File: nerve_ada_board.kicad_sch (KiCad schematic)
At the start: 55 parts, among them J2 TC2050-IDC, J3 2171750001, J4 Camera, J5 CAN1, J6 CAN2, J7 WS2812B, SW1 SPST, SW2 SPST, SW3 SPDT, SW4 SPST, U1 LD1117S33TR_SOT223, U2 STM32F446RET, U5 XBP9B-DMWT-002, U6 SAM-M10Q, U9 TXB0102DCT, Y1 8M, Y2 32.768K

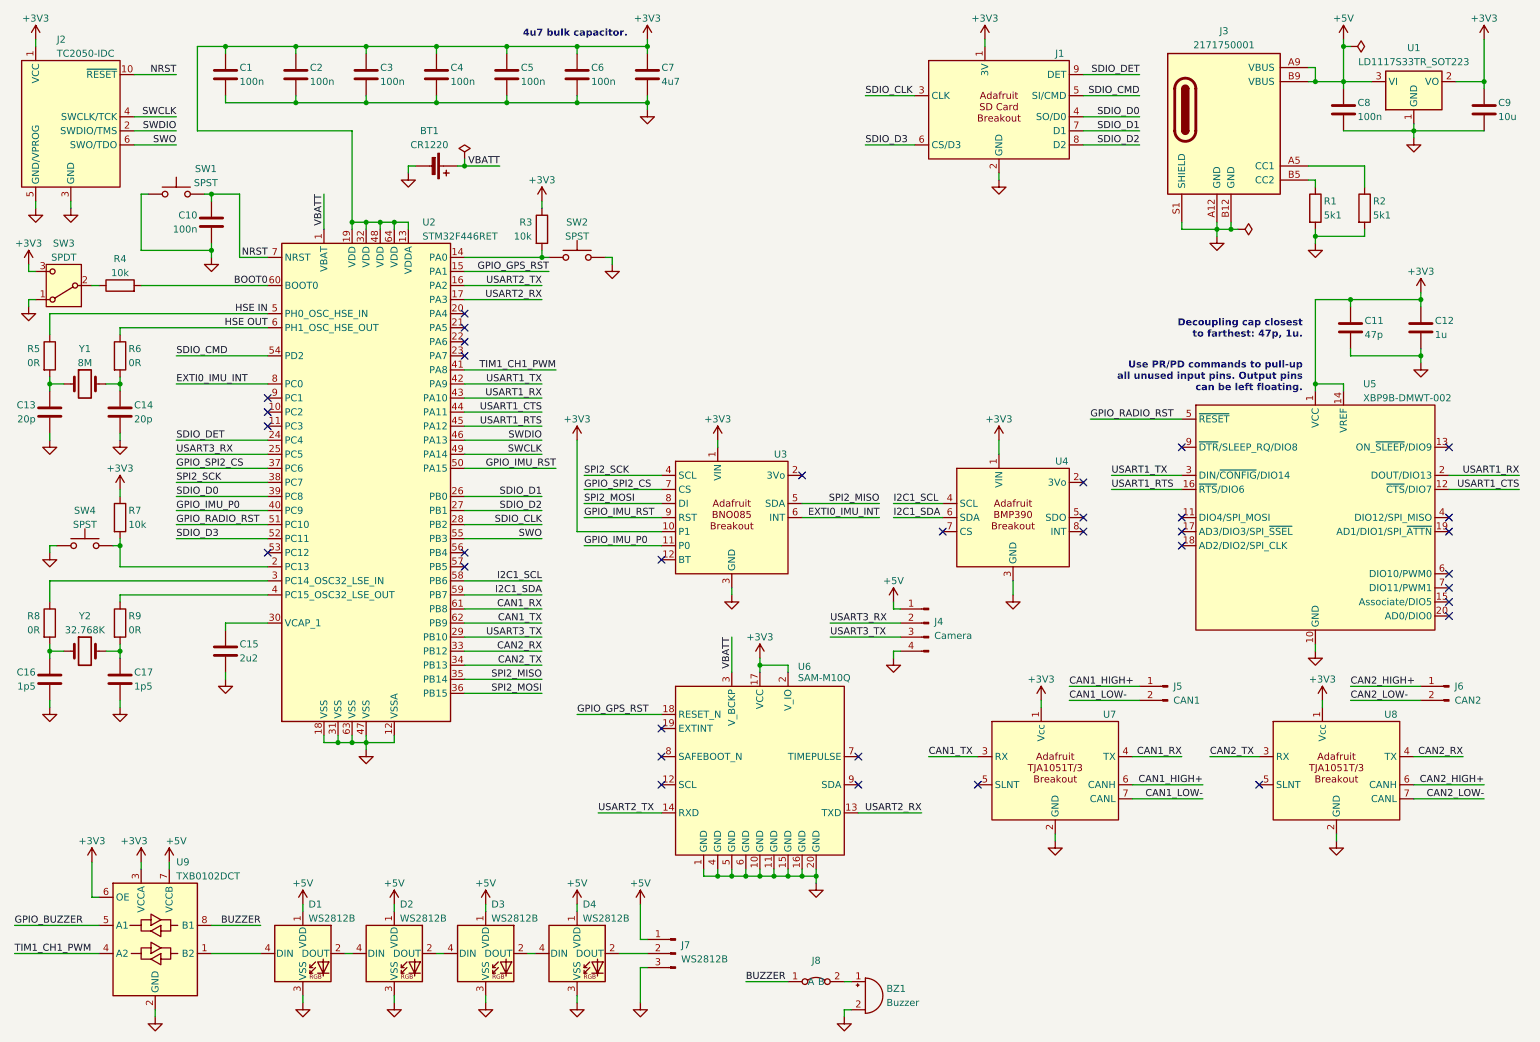
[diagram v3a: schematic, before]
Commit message: Pass ERC, add final MCU breakouts, clean up
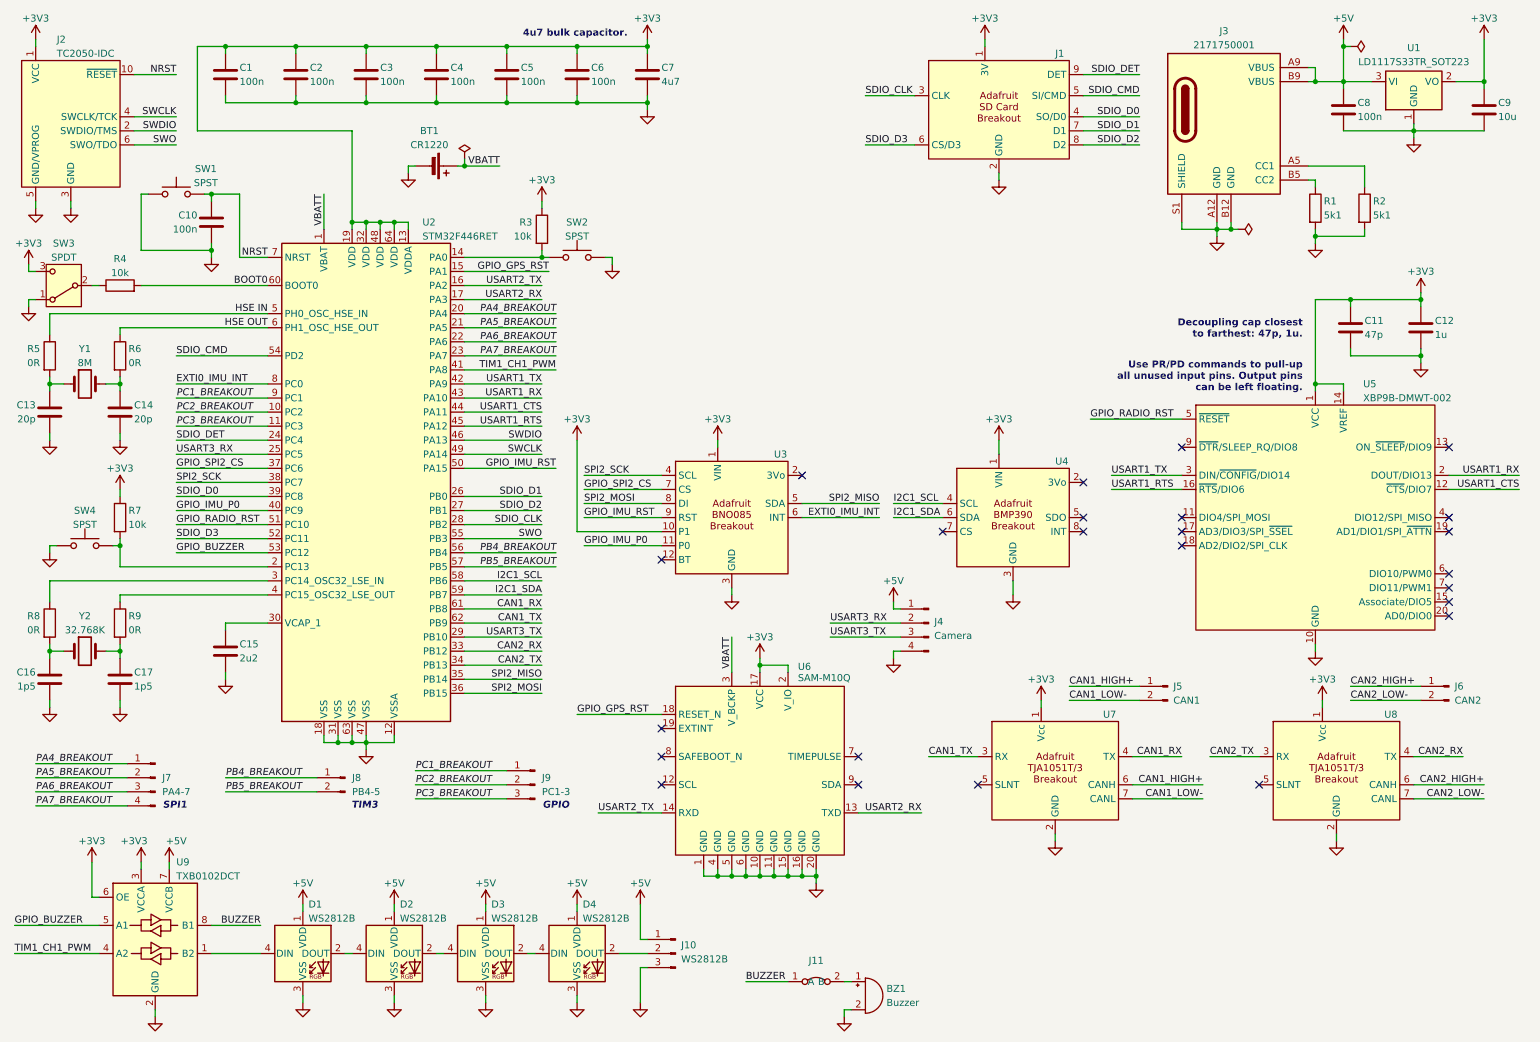
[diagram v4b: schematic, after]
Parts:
- added J7: PA4-7, symbol Connector:Conn_01x04_Pin
- added J8: PB4-5, symbol Connector:Conn_01x02_Pin
- added J9: PC1-3, symbol Connector:Conn_01x03_Pin
- renumbered J7 to J10, J8 to J11
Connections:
- net GPIO_BUZZER: now also U2.53 (PC12)
- net PC2_BREAKOUT: now reaches U2.10 (PC2)
- net PC2_BREAKOUT: now also J9.2 (Pin_2)
- net PC3_BREAKOUT: now reaches U2.11 (PC3)
- net PC3_BREAKOUT: now also J9.3 (Pin_3)
- net PA4_BREAKOUT: now reaches U2.20 (PA4)
- net PA4_BREAKOUT: now also J7.1 (Pin_1)
- net PA5_BREAKOUT: now reaches U2.21 (PA5)
- net PA5_BREAKOUT: now also J7.2 (Pin_2)
- net PA6_BREAKOUT: now reaches U2.22 (PA6)
- net PA6_BREAKOUT: now also J7.3 (Pin_3)
- net PA7_BREAKOUT: now reaches U2.23 (PA7)
- net PA7_BREAKOUT: now also J7.4 (Pin_4)
- net PB4_BREAKOUT: now reaches U2.56 (PB4)
- net PB4_BREAKOUT: now also J8.1 (Pin_1)
- net PB5_BREAKOUT: now reaches U2.57 (PB5)
- net PB5_BREAKOUT: now also J8.2 (Pin_2)
- net PC1_BREAKOUT: now reaches U2.9 (PC1)
- net PC1_BREAKOUT: now also J9.1 (Pin_1)
- no-connect marks 34 -> 24
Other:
- note added: "GPIO"
- note added: "SPI1"
- note added: "TIM3"

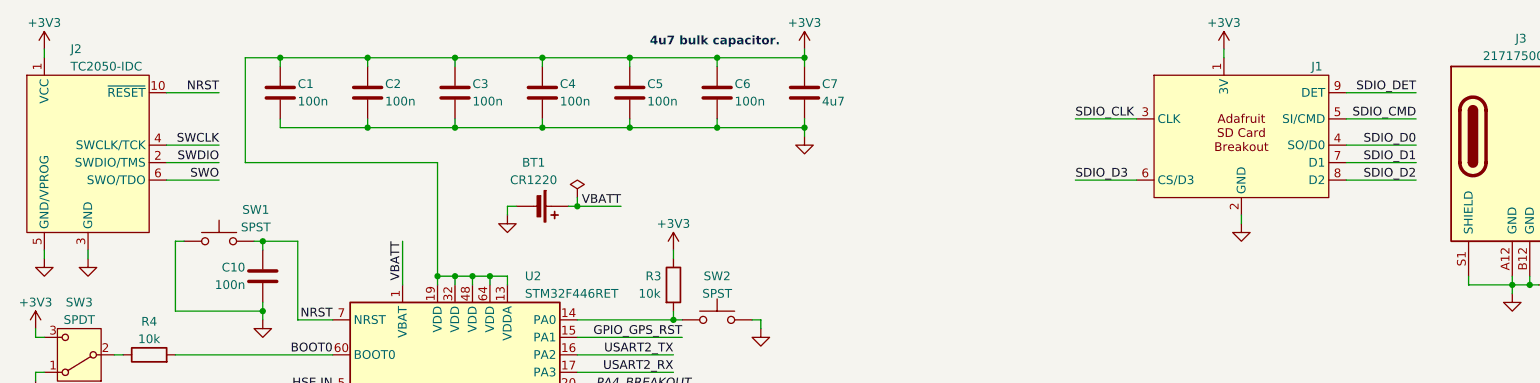
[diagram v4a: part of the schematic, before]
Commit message: Clean up REF annotation sequence
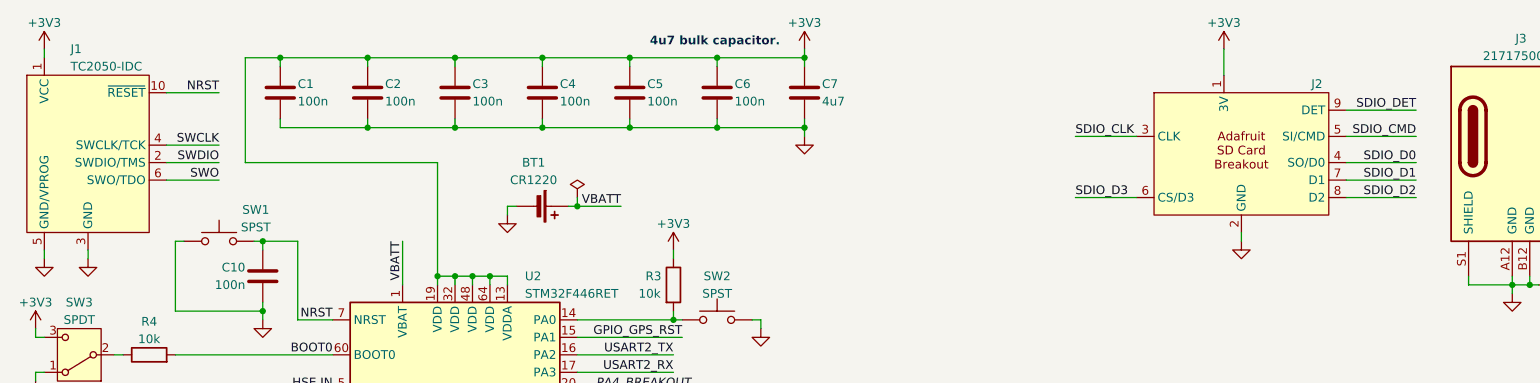
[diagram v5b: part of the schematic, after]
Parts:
- renumbered J2 to J1, J1 to J2
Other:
- moved on the sheet: J2
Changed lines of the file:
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@@
 	(wire
 		(pts
-			(xy 166.37 27.94) (xy 175.26 27.94)
+			(xy 166.37 30.48) (xy 175.26 30.48)
 		)
 		(stroke
@@
 	(wire
 		(pts
-			(xy 205.74 34.29) (xy 215.9 34.29)
+			(xy 205.74 36.83) (xy 215.9 36.83)
 		)
 		(stroke
@@
 	(wire
 		(pts
-			(xy 205.74 24.13) (xy 215.9 24.13)
+			(xy 205.74 26.67) (xy 215.9 26.67)
 		)
 		(stroke
@@
 	(wire
 		(pts
-			(xy 166.37 36.83) (xy 175.26 36.83)
+			(xy 166.37 39.37) (xy 175.26 39.37)
 		)
 		(stroke
@@
 	(wire
 		(pts
-			(xy 187.96 17.78) (xy 187.96 19.05)
+			(xy 187.96 17.78) (xy 187.96 21.59)
 		)
 		(stroke
@@
 	(wire
 		(pts
-			(xy 205.74 36.83) (xy 215.9 36.83)
+			(xy 205.74 39.37) (xy 215.9 39.37)
 		)
 		(stroke
@@
 	(wire
 		(pts
-			(xy 205.74 31.75) (xy 215.9 31.75)
+			(xy 205.74 34.29) (xy 215.9 34.29)
 		)
 		(stroke
@@
 	(wire
 		(pts
-			(xy 205.74 27.94) (xy 215.9 27.94)
+			(xy 205.74 30.48) (xy 215.9 30.48)
 		)
 		(stroke
@@
 	(wire
 		(pts
-			(xy 190.5 41.91) (xy 190.5 43.18)
+			(xy 190.5 44.45) (xy 190.5 45.72)
 		)
 		(stroke
@@
 	)
 	(label "SDIO_DET"
-		(at 215.9 24.13 180)
+		(at 215.9 26.67 180)
 		(fields_autoplaced yes)
 		(effects
@@
 	)
 	(label "SDIO_D1"
-		(at 215.9 34.29 180)
+		(at 215.9 36.83 180)
 		(fields_autoplaced yes)
 		(effects
@@
 	)
 	(label "SDIO_D3"
-		(at 166.37 36.83 0)
+		(at 166.37 39.37 0)
 		(fields_autoplaced yes)
 		(effects
@@
 	)
 	(label "SDIO_CMD"
-		(at 215.9 27.94 180)
+		(at 215.9 30.48 180)
 		(fields_autoplaced yes)
 		(effects
@@
 	)
 	(label "SDIO_CLK"
-		(at 166.37 27.94 0)
+		(at 166.37 30.48 0)
 		(fields_autoplaced yes)
 		(effects
@@
 	)
 	(label "SDIO_D2"
-		(at 215.9 36.83 180)
+		(at 215.9 39.37 180)
 		(fields_autoplaced yes)
 		(effects
@@
 	)
 	(label "SDIO_D0"
-		(at 215.9 31.75 180)
+		(at 215.9 34.29 180)
 		(fields_autoplaced yes)
 		(effects
@@
 	(symbol
 		(lib_id "power:GND")
-		(at 190.5 43.18 0)
+		(at 190.5 45.72 0)
 		(unit 1)
 		(exclude_from_sim no)
@@
 		(fields_autoplaced yes)
 		(property "Reference" "#PWR09"
-			(at 190.5 49.53 0)
+			(at 190.5 52.07 0)
 			(effects
 				(font
@@
 		)
 		(property "Value" "GND"
-			(at 190.5 48.26 0)
+			(at 190.5 50.8 0)
 			(effects
 				(font
@@
 		)
 		(property "Footprint" ""
-			(at 190.5 43.18 0)
+			(at 190.5 45.72 0)
 			(effects
 				(font
@@
 		)
 		(property "Datasheet" ""
-			(at 190.5 43.18 0)
+			(at 190.5 45.72 0)
 			(effects
 				(font
@@
 		)
 		(property "Description" "Power symbol creates a global label with name \"GND\" , ground"
-			(at 190.5 43.18 0)
+			(at 190.5 45.72 0)
 			(effects
 				(font
@@
 		(on_board yes)
 		(dnp no)
-		(property "Reference" "J2"
+		(property "Reference" "J1"
 			(at 20.32 17.78 0)
 			(effects
@@
 			(project ""
 				(path "/c0277862-b3f2-4e0e-986f-34702f0543f0"
-					(reference "J2")
+					(reference "J1")
 					(unit 1)
 				)
@@
 	(symbol
 		(lib_id "adafruit:adafruit_4682_sdio_card")
-		(at 190.5 30.48 0)
+		(at 190.5 33.02 0)
 		(unit 1)
 		(exclude_from_sim yes)
@@
 		(on_board yes)
 		(dnp no)
-		(property "Reference" "J1"
-			(at 200.66 20.32 0)
+		(property "Reference" "J2"
+			(at 200.66 22.86 0)
 			(effects
 				(font
@@
 		)
 		(property "Value" "~"
-			(at 190.1541 20.32 0)
+			(at 190.1541 22.86 0)
 			(effects
 				(font
@@
 		)
 		(property "Footprint" "adafruit:adafruit_4682_sdio_card"
-			(at 190.5 30.48 0)
+			(at 190.5 33.02 0)
 			(effects
 				(font
@@
 		)
 		(property "Datasheet" "https://learn.adafruit.com/adafruit-microsd-spi-sdio"
-			(at 190.5 30.48 0)
+			(at 190.5 33.02 0)
 			(effects
 				(font
@@
 		)
 		(property "Description" "Adafruit MicroSD SPI or SDIO Card Breakout Board"
-			(at 190.5 30.48 0)
+			(at 190.5 33.02 0)
 			(effects
 				(font
@@
 		)
 		(property "Manufacturer" "Adafruit"
-			(at 190.5 30.48 0)
+			(at 190.5 33.02 0)
 			(effects
 				(font
@@
 		)
 		(property "Manufacturer Part Number" "4682"
-			(at 190.5 30.48 0)
+			(at 190.5 33.02 0)
 			(effects
 				(font
@@
 		)
 		(property "Distributor" "DigiKey"
-			(at 190.5 30.48 0)
+			(at 190.5 33.02 0)
 			(effects
 				(font
@@
 		)
 		(property "Distributor Part Number" "1528-4682-ND"
-			(at 190.5 30.48 0)
+			(at 190.5 33.02 0)
 			(effects
 				(font
@@
 		)
 		(property "Distributor Link" "https://www.digikey.ca/en/products/detail/adafruit-industries-llc/4682/12822319?s=N4IgTCBcDaICwDYAcYAEBDAJugZgJwFcBLAFxAF0BfIA"
-			(at 190.5 30.48 0)
+			(at 190.5 33.02 0)
 			(effects
 				(font
@@
 			(project ""
 				(path "/c0277862-b3f2-4e0e-986f-34702f0543f0"
-					(reference "J1")
+					(reference "J2")
 					(unit 1)
 				)

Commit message: Update library and LSE crystal on schematic
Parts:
- removed Y2: 32.768K, symbol Device:Crystal
- added U6: 32k768, common:xtal_abs25-32.768khz-6-t, symbol common:abs25-32.768khz-6-t
- renumbered U9 to U10, U6 to U7, U7 to U8, U8 to U9
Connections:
- net at C16.1, R8.2: now also U6.1
- net at C17.1, R9.2: now also U6.2
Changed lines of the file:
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@@
 	)
 	(symbol
+		(lib_id "common:abs25-32.768khz-6-t")
+		(at 25.4 128.27 0)
+		(unit 1)
+		(exclude_from_sim no)
+		(in_bom yes)
+		(on_board yes)
+		(dnp no)
+		(fields_autoplaced yes)
+		(property "Reference" "U6"
+			(at 25.4 120.65 0)
+			(effects
+				(font
+					(size 1.27 1.27)
+				)
+			)
+		)
+		(property "Value" "32k768"
+			(at 25.4 123.19 0)
+			(effects
+				(font
+					(size 1.27 1.27)
+				)
+			)
+		)
+		(property "Footprint" "common:xtal_abs25-32.768khz-6-t"
+			(at 25.4 128.27 0)
+			(effects
+				(font
+					(size 1.27 1.27)
+				)
+				(hide yes)
+			)
+		)
+		(property "Datasheet" "https://abracon.com/Resonators/abs25.pdf"
+			(at 25.4 128.27 0)
+			(effects
+				(font
+					(size 1.27 1.27)
+				)
+				(hide yes)
+			)
+		)
+		(property "Description" "CRYSTAL 32.7680KHz 6PF SMD"
+			(at 25.4 128.27 0)
+			(effects
+				(font
+					(size 1.27 1.27)
+				)
+				(hide yes)
+			)
+		)
+		(property "Manufacturer" "Abracon LLC"
+			(at 25.4 128.27 0)
+			(effects
+				(font
+					(size 1.27 1.27)
+				)
+				(hide yes)
+			)
+		)
+		(property "Manufacturer Part Number" "ABS25-32.768KHZ-6-T"
+			(at 25.4 128.27 0)
+			(effects
+				(font
+					(size 1.27 1.27)
+				)
+				(hide yes)
+			)
+		)
+		(property "Distributor" "DigiKey"
+			(at 25.4 128.27 0)
+			(effects
+				(font
+					(size 1.27 1.27)
+				)
+				(hide yes)
+			)
+		)
+		(property "Distributor Part Number" "535-10240-1-ND"
+			(at 25.4 128.27 0)
+			(effects
+				(font
+					(size 1.27 1.27)
+				)
+				(hide yes)
+			)
+		)
+		(property "Distributor Link" "https://www.digikey.ca/en/products/detail/abracon-llc/ABS25-32-768KHZ-6-T/2217986"
+			(at 25.4 128.27 0)
+			(effects
+				(font
+					(size 1.27 1.27)
+				)
+				(hide yes)
+			)
+		)
+		(pin "2"
+		)
+		(pin "1"
+		)
+		(instances
+			(project ""
+				(path "/c0277862-b3f2-4e0e-986f-34702f0543f0"
+					(reference "U6")
+					(unit 1)
+				)
+			)
+		)
+	)
+	(symbol
 		(lib_id "Device:C")
 		(at 31.75 85.09 0)
@@
 	)
 	(symbol
-		(lib_id "Device:Crystal")
-		(at 25.4 128.27 0)
-		(unit 1)
-		(exclude_from_sim no)
-		(in_bom yes)
-		(on_board yes)
-		(dnp no)
-		(property "Reference" "Y2"
-			(at 25.4 121.92 0)
-			(effects
-				(font
-					(size 1.27 1.27)
-				)
-			)
-		)
-		(property "Value" "32.768K"
-			(at 25.4 124.46 0)
-			(effects
-				(font
-					(size 1.27 1.27)
-				)
-			)
-		)
-		(property "Footprint" ""
-			(at 25.4 128.27 0)
-			(effects
-				(font
-					(size 1.27 1.27)
-				)
-				(hide yes)
-			)
-		)
-		(property "Datasheet" "~"
-			(at 25.4 128.27 0)
-			(effects
-				(font
-					(size 1.27 1.27)
-				)
-				(hide yes)
-			)
-		)
-		(property "Description" "Two pin crystal"
-			(at 25.4 128.27 0)
-			(effects
-				(font
-					(size 1.27 1.27)
-				)
-				(hide yes)
-			)
-		)
-		(pin "1"
-		)
-		(pin "2"
-		)
-		(instances
-			(project "nerve_ada_board"
-				(path "/c0277862-b3f2-4e0e-986f-34702f0543f0"
-					(reference "Y2")
-					(unit 1)
-				)
-			)
-		)
-	)
-	(symbol
 		(lib_id "Device:R")
 		(at 31.75 74.93 0)
@@
 		(on_board yes)
 		(dnp no)
-		(property "Reference" "U7"
+		(property "Reference" "U8"
 			(at 209.296 139.7 0)
 			(effects
@@
 			(project "nerve_ada_board"
 				(path "/c0277862-b3f2-4e0e-986f-34702f0543f0"
-					(reference "U7")
+					(reference "U8")
 					(unit 1)
 				)
@@
 		(on_board yes)
 		(dnp no)
-		(property "Reference" "U6"
+		(property "Reference" "U7"
 			(at 154.178 131.064 0)
 			(effects
@@
 			(project ""
 				(path "/c0277862-b3f2-4e0e-986f-34702f0543f0"
-					(reference "U6")
+					(reference "U7")
 					(unit 1)
 				)
@@
 		(on_board yes)
 		(dnp no)
-		(property "Reference" "U9"
+		(property "Reference" "U10"
 			(at 41.91 166.37 0)
 			(effects
@@
 			(project ""
 				(path "/c0277862-b3f2-4e0e-986f-34702f0543f0"
-					(reference "U9")
+					(reference "U10")
 					(unit 1)
 				)
@@
 		(on_board yes)
 		(dnp no)
-		(property "Reference" "U8"
+		(property "Reference" "U9"
 			(at 260.096 139.7 0)
 			(effects
@@
 			(project "nerve_ada_board"
 				(path "/c0277862-b3f2-4e0e-986f-34702f0543f0"
-					(reference "U8")
+					(reference "U9")
 					(unit 1)
 				)
